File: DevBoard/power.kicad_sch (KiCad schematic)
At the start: 31 parts, among them J201 SMA OUT_LO, J202 SMA OUT_HI, U201 INA190A5IDDFR, U202 INA190A1IDDFR, U203 TPS70950DBVR, U204 TPS62177DQCR

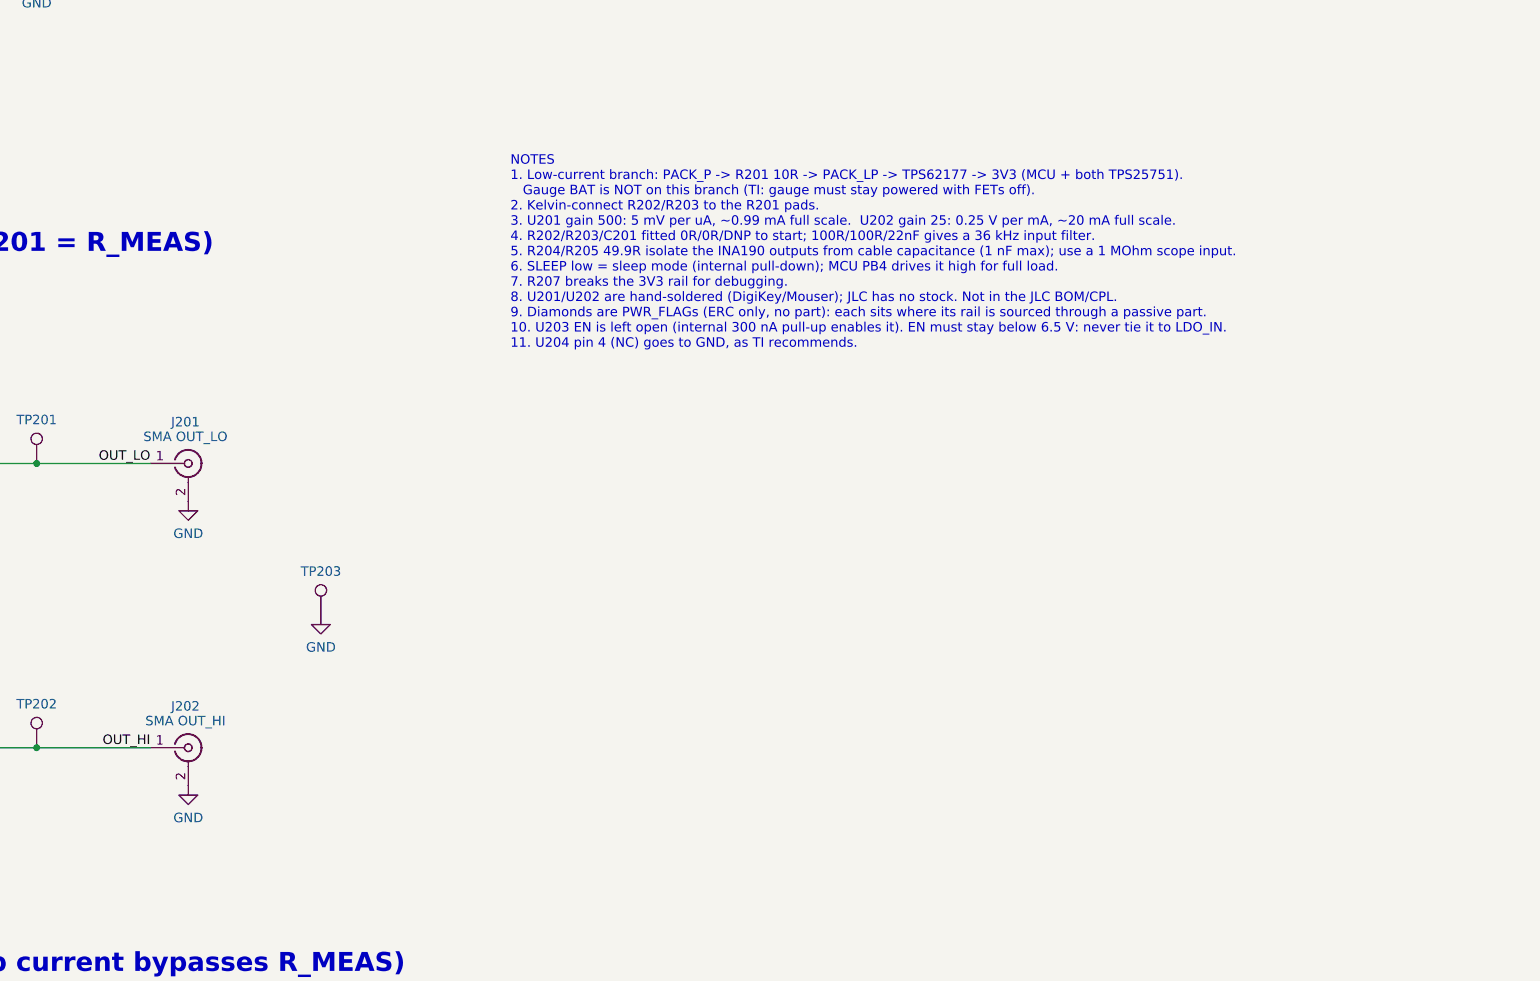
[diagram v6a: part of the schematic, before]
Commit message: Dev board: silkscreen purpose/pinout labels; sleep-current SMAs to test loops
- Silkscreen: WAKE / RESET / AMP EN / MEAS PWR / SWD part labels and pin
  labels on J101, J102-J107, J103, J104, J303, J402/J502, J301 pin 1
  (place_parts.py PIN_LABELS / PART_LABELS; README item 30).
- J201/J202 vertical SMAs removed: OUT_LO/OUT_HI probed on TP201/TP202, each
  with a GND loop (TP208/TP209) 4.5 mm away, in a row on the bottom edge.
  R204/R205 49.9R kept (README item 31; docs updated).
- Renders, 2D exports and schematic PDF regenerated.

Co-Authored-By: Claude Opus 5.5 <noreply@anthropic.com>
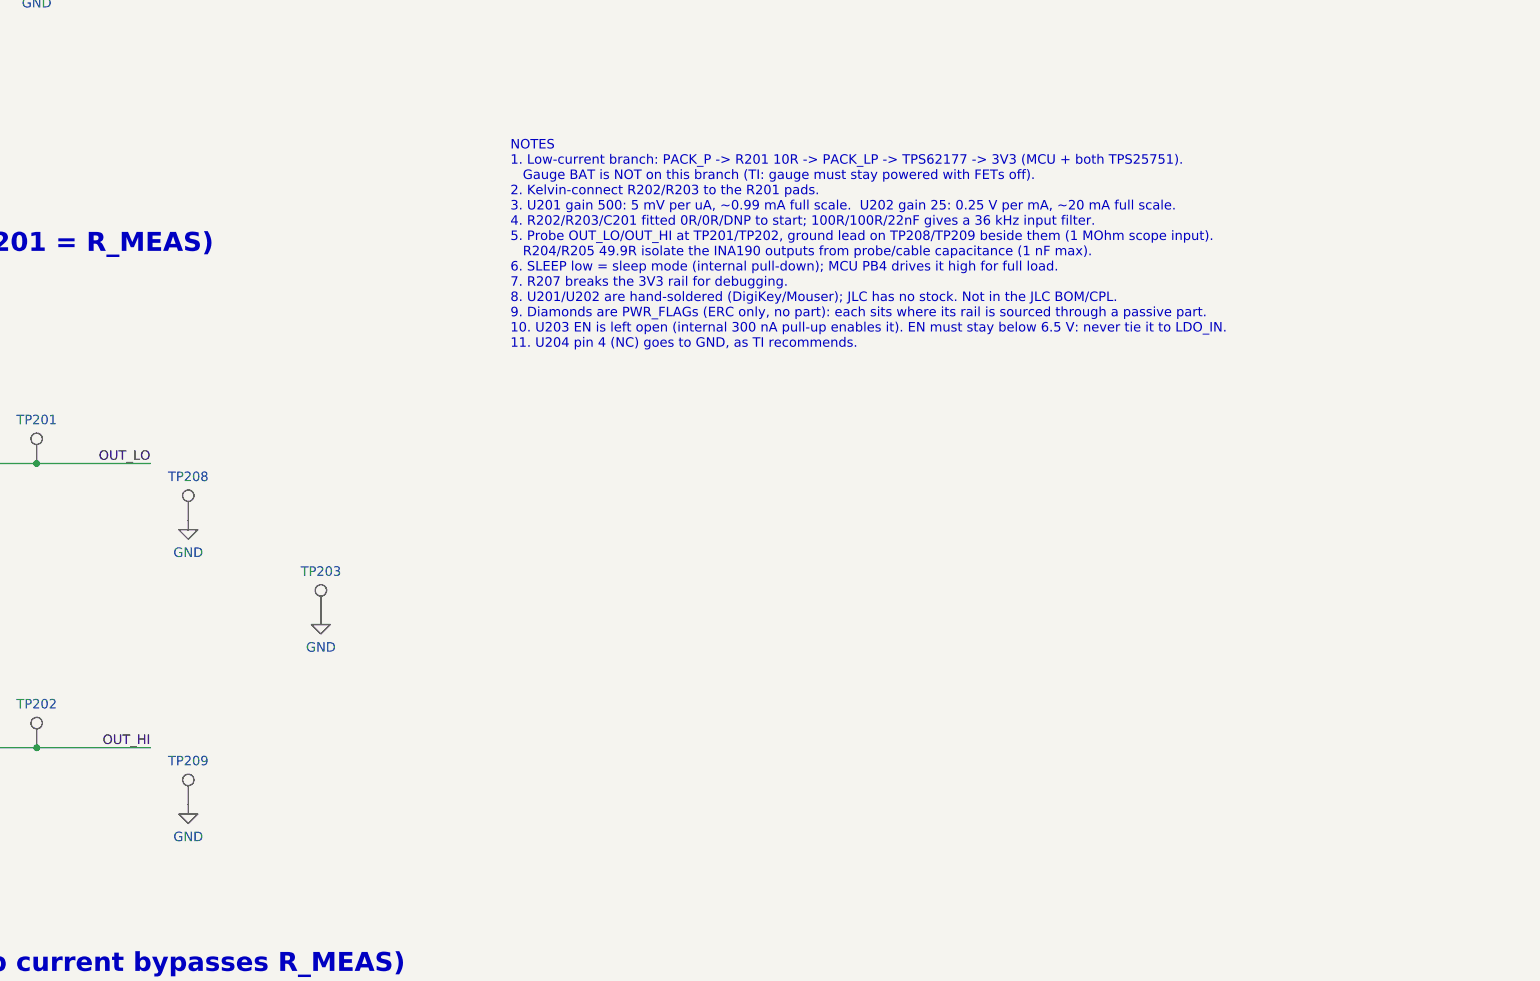
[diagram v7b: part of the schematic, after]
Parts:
- removed J201: SMA OUT_LO, Connector_Coaxial:SMA_Amphenol_132134_Vertical, symbol Connector:Conn_Coaxial
- removed J202: SMA OUT_HI, Connector_Coaxial:SMA_Amphenol_132134_Vertical, symbol Connector:Conn_Coaxial
- added TP208, TP209: GND, MonolithDev:TestPoint_Harwin_S2761_0603, symbol Connector:TestPoint
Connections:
- net GND: now also TP208.1, TP209.1

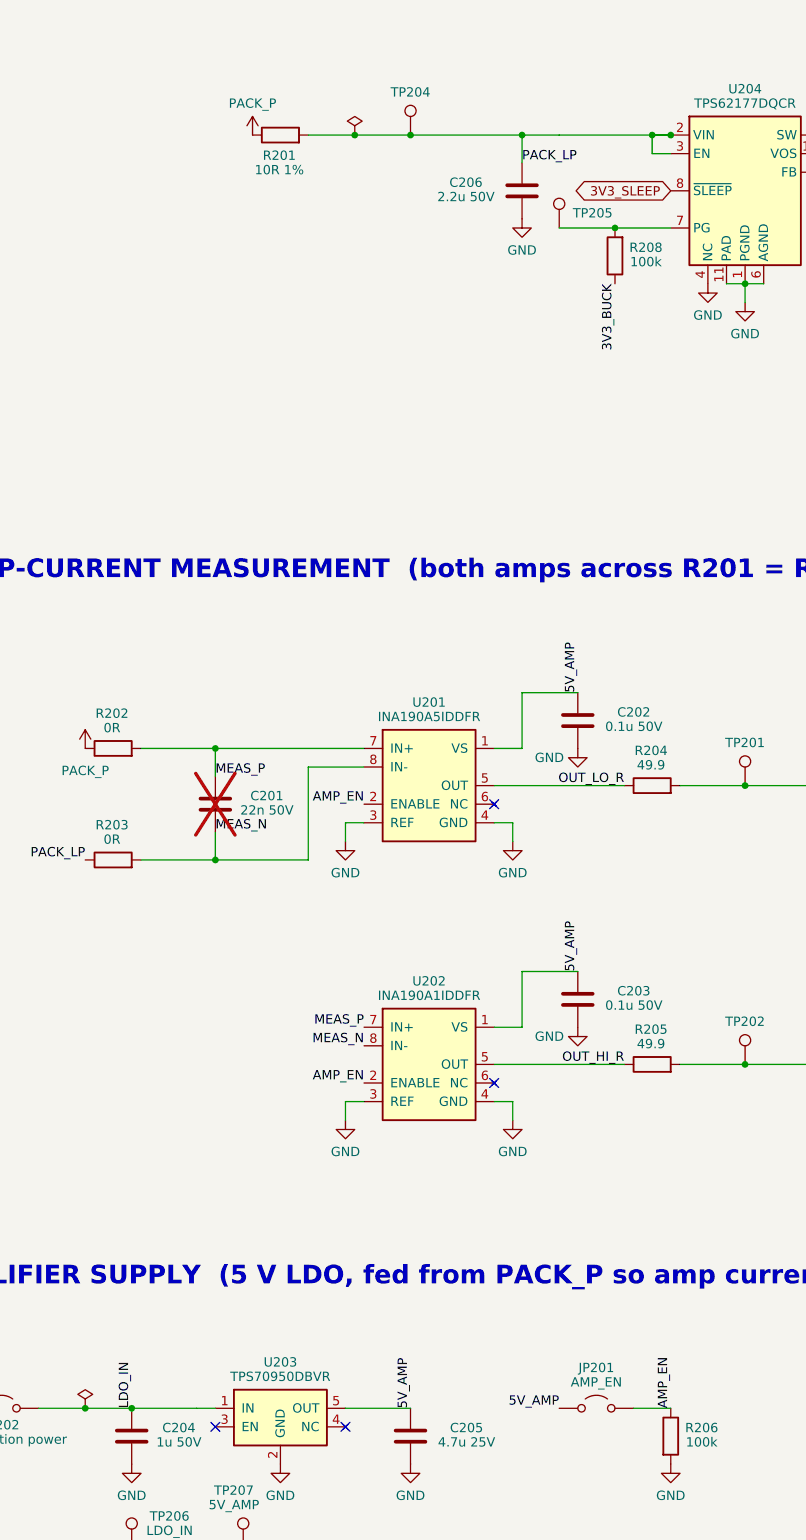
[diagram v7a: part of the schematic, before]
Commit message: Dev board: second-level pack protection, D103 fitted, U202 JLC, strap cleanup
- Gauge sheet: BQ294700 (4.35 V/cell OVP) and the BQ40Z50 FUSE pin share
  ignition FET Q104 (TI BQ40Z50-R2 fig. 9-11) to blow F102, a TLC WSFB1514
  4-cell 15 A self-control fuse at the cell top. F101 removed: F102 is the
  pack fuse. R127 DNP bench bypass. New symbols/footprint/3D model.
- D103 (Q102 gate-source 15 V clamp) fitted on dev board and production.
- U202 INA190A1 now JLC-assembled (C1852068); U201 stays hand-soldered.
- TPS25751 ADCIN divider footprints R405-R408 removed (SafeMode 0x20/0x21
  needs only the R1-R4 ties); place_parts rows and notes updated.
- Layout not yet updated for these changes.

Co-Authored-By: Claude Opus 5.5 <noreply@anthropic.com>
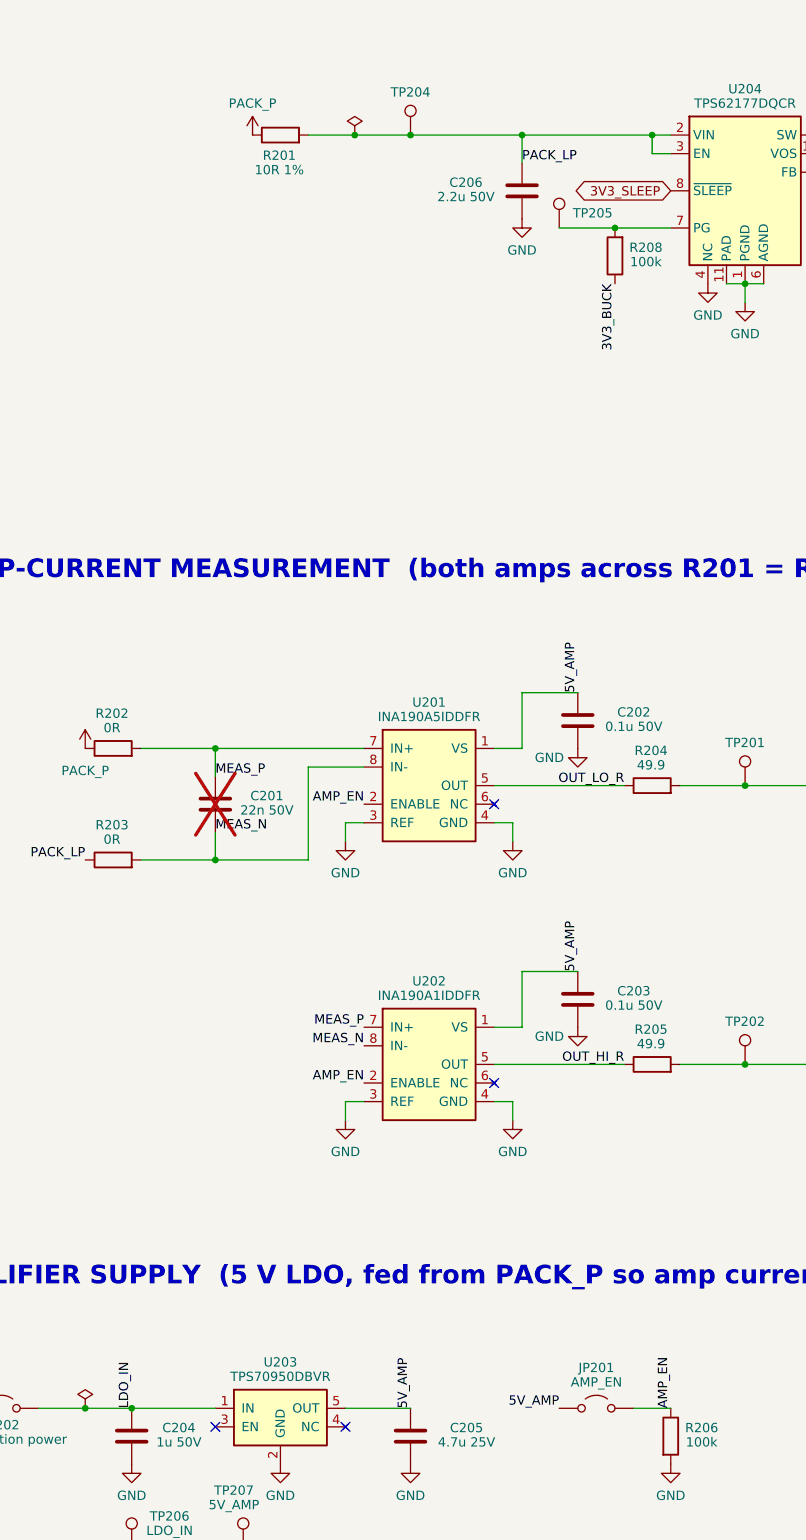
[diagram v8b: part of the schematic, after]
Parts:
- U202: LCSC (none) -> C1852068; Sourcing DigiKey/Mouser, hand-solder (not JLC assembled) -> JLC assembled (LCSC C1852068, 1,700 in stock 2026-10-13)
